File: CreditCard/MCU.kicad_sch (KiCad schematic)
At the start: 21 parts, among them J2 MEM2052-00-195-00-A_REVA, U3 PTS645SK43SMTR92LFS, U4 PTS645SK43SMTR92LFS, U8 ESP32-C6-WROOM-1U-N4, X1 MS1V-T1K-32.768KHZ-12.5PF-20P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

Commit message: manque écran
manque seulement l'écran le reste est ajouter
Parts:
- removed J2: MEM2052-00-195-00-A_REVA, LIB:GCT_MEM2052-00-195-00-A_REVA, symbol MEM2052-00-195-00-A_REVA:MEM2052-00-195-00-A_REVA
- removed U8: ESP32-C6-WROOM-1U-N4, LIB:XCVR_ESP32-C6-WROOM-1U-N4, symbol ESP32-C6-WROOM-1U-N4:ESP32-C6-WROOM-1U-N4
- removed X1: MS1V-T1K-32.768KHZ-12.5PF-20PPM-TA-QC, LIB:XTAL_MS1V-T1K-32.768KHZ-12.5PF-20PPM-TA-QC, symbol LIB:MS1V-T1K-32.768KHZ-12.5PF-20PPM-TA-QC
- added J2: MEM2052-00-195-00-A_REVA, Library:GCT_MEM2052-00-195-00-A_REVA, symbol Library:MEM2052-00-195-00-A_REVA
- added U8: ESP32-C6-WROOM-1U-N4, Library:XCVR_ESP32-C6-WROOM-1U-N4, symbol Library:ESP32-C6-WROOM-1U-N4
- added Y1: MS1V-T1K-32.768KHZ-12.5PF-20PPM-TA-QC, Library:XTAL_MS1V-T1K-32.768KHZ-12.5PF-20PPM-TA-QC, symbol Library:MS1V-T1K-32.768KHZ-12.5PF-20PPM-TA-QC
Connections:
- net 3V3: now also J2.P4 (VDD), U8.2 (3V3)
- net CS_SD: now also J2.P2 (CD/DAT3), U8.20 (IO22)
- net CardDetect_SD: now also J2.P9 (CD_PIN), U8.19 (IO21)
- net D_N: now also U8.13 (IO12)
- net D_P: now also U8.14 (IO13)
- net GND: now also J2.G1 (SHIELD_GND), J2.G2 (SHIELD_GND), J2.G3 (SHIELD_GND), J2.G4 (SHIELD_GND), J2.P6 (VSS), U8.1 (GND), U8.28 (GND__1), U8.29_1 (GND__2), U8.29_2 (GND__3), U8.29_3 (GND__4), U8.29_4 (GND__5), U8.29_5 (GND__6), U8.29_6 (GND__7), U8.29_7 (GND__8), U8.29_8 (GND__9), U8.29_9 (GND__10)
- net GPIO2: now also U8.27 (IO2)
- net GPIO3: now also U8.26 (IO3)
- net GPIO4: now also U8.4 (IO4)
- net GPIO5: now also U8.5 (IO5)
- net GPIO6: now also U8.6 (IO6)
- net GPIO7: now also U8.7 (IO7)
- net IO9: now also U8.15 (IO9)
- net IO_CHG: now also U8.21 (IO23)
- net MCU_EN: now also U8.3 (EN)
- net MISO: now also J2.P7 (DAT0), U8.16 (IO18)
- net MOSI: now also J2.P3 (CMD), U8.17 (IO19)
- net SCK: now also J2.P5 (CLK), U8.11 (IO10)
- net SCL: now also U8.25 (TXD0/GPIO16)
- net SDA: now also U8.24 (RXD0/GPIO17)
- net XTAL_N: now also U8.8 (IO0)
- net XTAL_P: now also U8.9 (IO1)
- net at C12.1, R14.2, R17.2: now also Y1.1
- net at C17.1, R17.1, R20.2: now also Y1.2
- net at R2.1: now also U8.10 (IO8)

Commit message: ajout des gold fingers
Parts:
- removed F1, F2, F4, F5, F6: ~, CommonLib_HORUS:GOLD_FINGERS, symbol LIB:GoldFingers
- added F1, F2, F3, F4: ~, Library:GOLD_FINGERS, symbol Library:GoldFingers
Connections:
- net 3V3: now also F4.1 (GOLDFINGER)
- net IO_CHG: now also F3.1 (GOLDFINGER)
- net SCL: now also F2.1 (GOLDFINGER)
- net SDA: now also F1.1 (GOLDFINGER)

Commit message: connection du audio amp
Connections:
- net SCK: now also U8.23 (IO15); no longer U8.11 (IO10)
- net AudioR: now reaches U8.12 (IO11)
- net AudioCS: now reaches U8.18 (IO20)
- new net AudioL: U8.11 (IO10)
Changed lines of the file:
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@@
+		)
+	)
+	(global_label "AudioL"
+		(shape output)
+		(at 185.42 48.26 0)
+		(fields_autoplaced yes)
+		(effects
+			(font
+				(size 1.27 1.27)
+			)
+			(justify left)
+		)
+		(property "Intersheetrefs" "${INTERSHEET_REFS}"
+			(at 194.5737 48.26 0)
+			(effects
+				(font
+					(size 1.27 1.27)
+				)
+				(justify left)
+				(hide yes)
+			)
 		)
 	)
@@
 		)
 	)
+	(global_label "SCK"
+		(shape output)
+		(at 185.42 58.42 0)
+		(fields_autoplaced yes)
+		(effects
+			(font
+				(size 1.27 1.27)
+			)
+			(justify left)
+		)
+		(property "Intersheetrefs" "${INTERSHEET_REFS}"
+			(at 192.1547 58.42 0)
+			(effects
+				(font
+					(size 1.27 1.27)
+				)
+				(justify left)
+				(hide yes)
+			)
+		)
+	)
 	(global_label "CardDetect_SD"
 		(shape output)
@@
 		)
 	)
+	(global_label "AudioR"
+		(shape output)
+		(at 185.42 50.8 0)
+		(fields_autoplaced yes)
+		(effects
+			(font
+				(size 1.27 1.27)
+			)
+			(justify left)
+		)
+		(property "Intersheetrefs" "${INTERSHEET_REFS}"
+			(at 194.8156 50.8 0)
+			(effects
+				(font
+					(size 1.27 1.27)
+				)
+				(justify left)
+				(hide yes)
+			)
+		)
+	)
 	(global_label "IO_CHG"
 		(shape input)
@@
 		)
 	)
-	(global_label "SCK"
-		(shape output)
-		(at 185.42 48.26 0)
-		(fields_autoplaced yes)
-		(effects
-			(font
-				(size 1.27 1.27)
-			)
-			(justify left)
-		)
-		(property "Intersheetrefs" "${INTERSHEET_REFS}"
-			(at 192.1547 48.26 0)
-			(effects
-				(font
-					(size 1.27 1.27)
-				)
-				(justify left)
-				(hide yes)
-			)
-		)
-	)
 	(global_label "MCU_EN"
 		(shape output)
@@
 				(hide yes)
 			)
+		)
+	)
+	(global_label "AudioCS"
+		(shape output)
+		(at 185.42 71.12 0)
+		(fields_autoplaced yes)
+		(effects
+			(font
+				(size 1.27 1.27)
+			)
+			(justify left)
+		)
+		(property "Intersheetrefs" "${INTERSHEET_REFS}"
+			(at 196.0251 71.12 0)
+			(effects
+				(font
+					(size 1.27 1.27)
+				)
+				(justify left)
+				(hide yes)
+			)

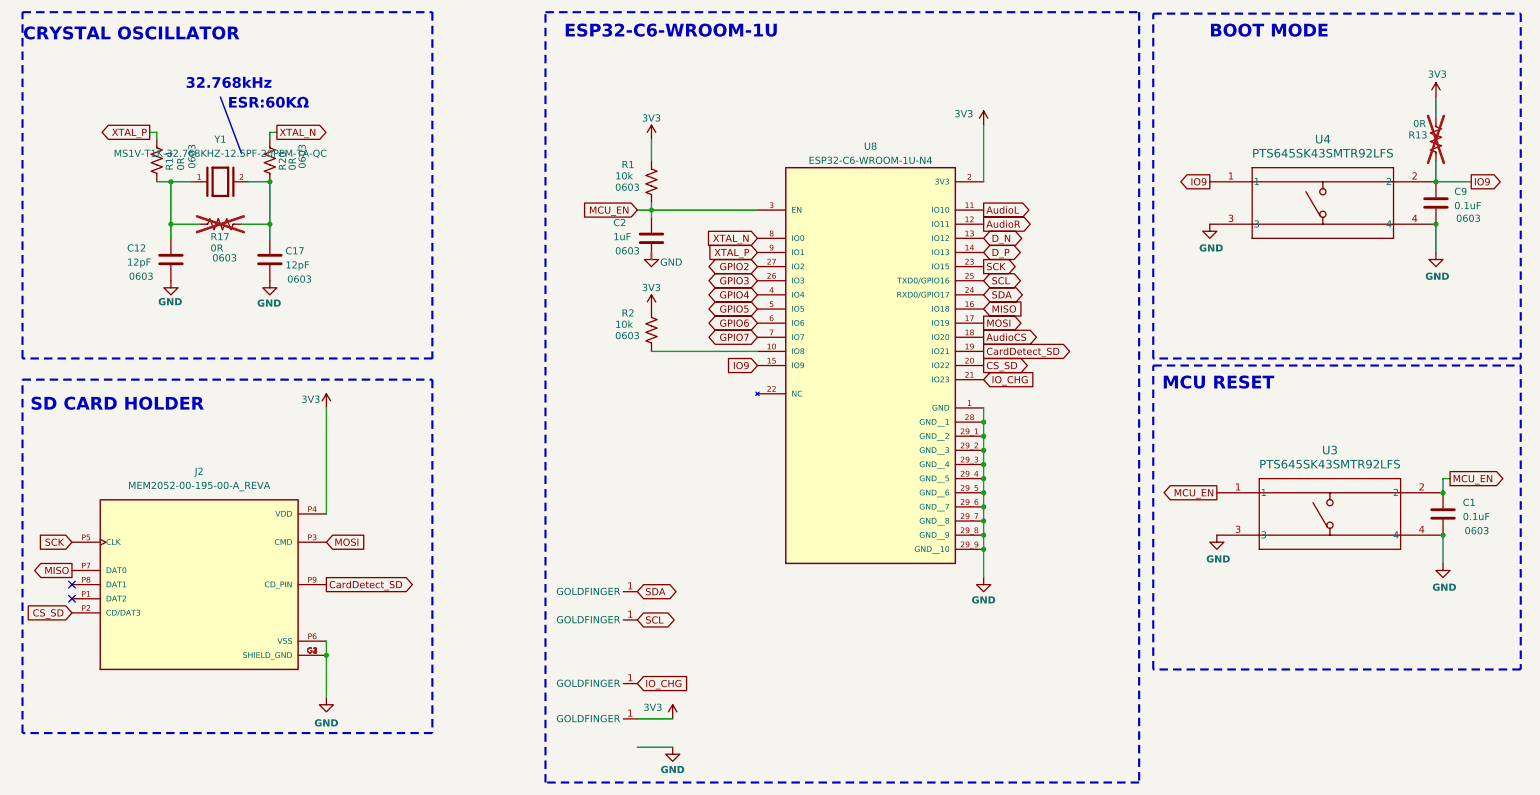
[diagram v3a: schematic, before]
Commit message: ajout du LCD
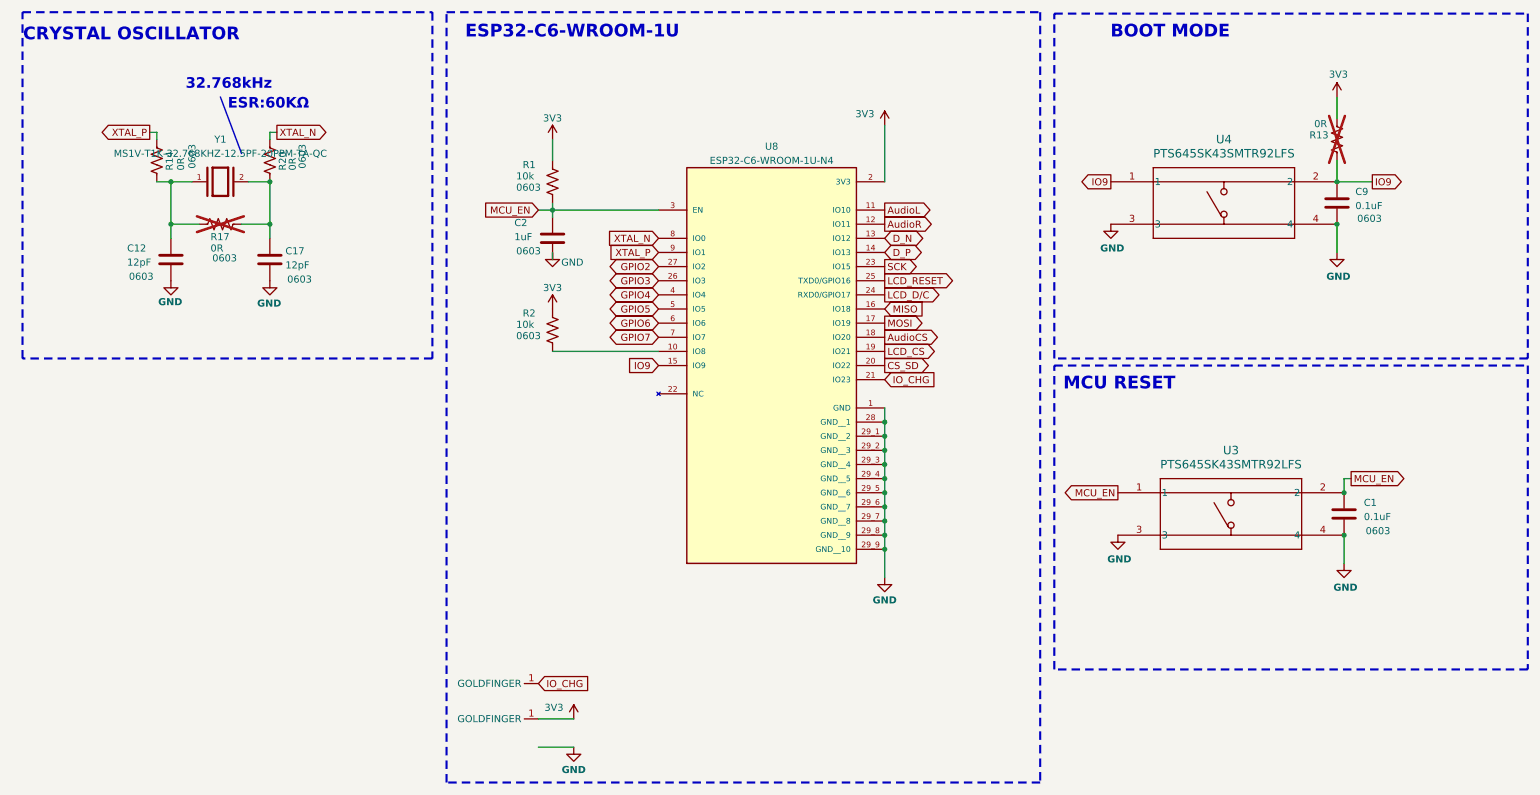
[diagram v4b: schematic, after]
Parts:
- removed F1, F2: ~, Library:GOLD_FINGERS, symbol Library:GoldFingers
- removed J2: MEM2052-00-195-00-A_REVA, Library:GCT_MEM2052-00-195-00-A_REVA, symbol Library:MEM2052-00-195-00-A_REVA
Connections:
- net CardDetect_SD renamed LCD_CS
- net SCL renamed LCD_RESET
- net SDA renamed LCD_D/C
- no-connect marks 2 -> 0
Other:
- note removed: "SD CARD HOLDER"
- moved on the sheet: C1, C2, C9, R1, R13, R2, U3, U4, U8

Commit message: rooting presque fini
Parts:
- removed R14, R20: 0R, Resistor_SMD:R_0603_1608Metric, symbol Device:R_US
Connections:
- net XTAL_N: now also C17.1, R17.1, Y1.2
- net XTAL_P: now also C12.1, R17.2, Y1.1

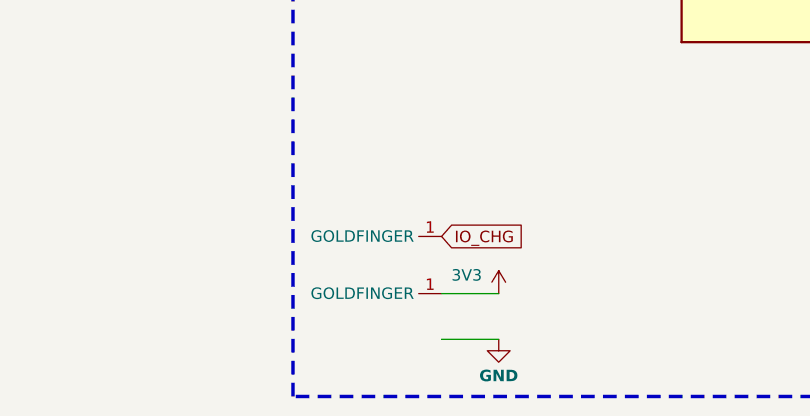
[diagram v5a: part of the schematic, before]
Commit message: gerber crée
pcb terminer
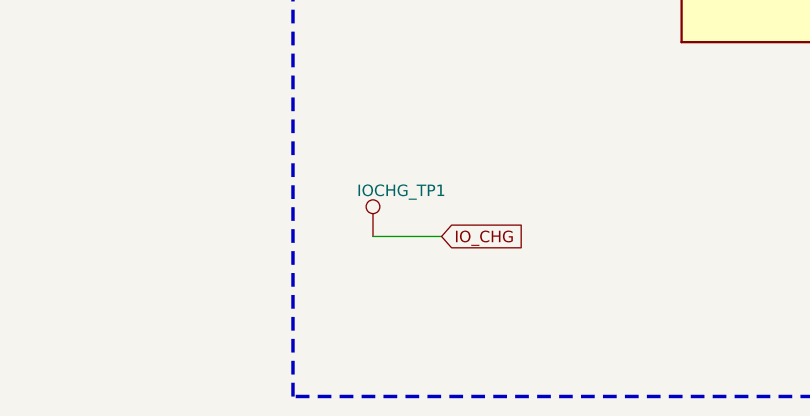
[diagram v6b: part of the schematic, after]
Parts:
- removed F3, F4: ~, Library:GOLD_FINGERS, symbol Library:GoldFingers
- added IOCHG_TP1: TP, TestPoint:TestPoint_Pad_D1.5mm, symbol Connector:TestPoint
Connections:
- net IO_CHG: now also IOCHG_TP1.1
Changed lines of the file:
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@@
 	(wire
 		(pts
-			(xy 107.95 73.66) (xy 127 73.66)
+			(xy 97.79 133.35) (xy 105.41 133.35)
 		)
 		(stroke
@@
 	(wire
 		(pts
-			(xy 248.92 27.94) (xy 248.92 31.75)
+			(xy 107.95 73.66) (xy 127 73.66)
 		)
 		(stroke
@@
 	(wire
 		(pts
-			(xy 248.92 43.18) (xy 255.27 43.18)
+			(xy 248.92 27.94) (xy 248.92 31.75)
 		)
 		(stroke
@@
 	(wire
 		(pts
-			(xy 39.37 43.18) (xy 43.18 43.18)
+			(xy 248.92 43.18) (xy 255.27 43.18)
 		)
 		(stroke
@@
 	(wire
 		(pts
-			(xy 167.64 101.6) (xy 167.64 104.14)
+			(xy 39.37 43.18) (xy 43.18 43.18)
 		)
 		(stroke
@@
 	(wire
 		(pts
-			(xy 251.46 96.52) (xy 250.19 96.52)
+			(xy 167.64 101.6) (xy 167.64 104.14)
 		)
 		(stroke
@@
 	(wire
 		(pts
-			(xy 167.64 106.68) (xy 167.64 109.22)
+			(xy 251.46 96.52) (xy 250.19 96.52)
 		)
 		(stroke
@@
 	(wire
 		(pts
-			(xy 111.76 139.7) (xy 105.41 139.7)
+			(xy 167.64 106.68) (xy 167.64 109.22)
 		)
 		(stroke
@@
 	(wire
 		(pts
-			(xy 105.41 144.78) (xy 111.76 144.78)
-		)
-		(stroke
-			(width 0)
-			(type default)
-		)
-	)
-	(wire
-		(pts
 			(xy 107.95 57.15) (xy 107.95 55.88)
 		)
@@
 	)
 	(symbol
-		(lib_id "power:+3.3V")
-		(at 111.76 139.7 0)
-		(unit 1)
-		(exclude_from_sim no)
-		(in_bom yes)
-		(on_board yes)
-		(dnp no)
-		(property "Reference" "#PWR032"
-			(at 111.76 143.51 0)
-			(effects
-				(font
-					(size 1.27 1.27)
-				)
-				(hide yes)
-			)
-		)
-		(property "Value" "3V3"
-			(at 108.204 137.668 0)
-			(effects
-				(font
-					(size 1.27 1.27)
-				)
-			)
-		)
-		(property "Footprint" ""
-			(at 111.76 139.7 0)
-			(effects
-				(font
-					(size 1.27 1.27)
-				)
-				(hide yes)
-			)
-		)
-		(property "Datasheet" ""
-			(at 111.76 139.7 0)
-			(effects
-				(font
-					(size 1.27 1.27)
-				)
-				(hide yes)
-			)
-		)
-		(property "Description" "Power symbol creates a global label with name \"+3.3V\""
-			(at 111.76 139.7 0)
-			(effects
-				(font
-					(size 1.27 1.27)
-				)
-				(hide yes)
-			)
-		)
-		(pin "1"
-		)
-		(instances
-			(project "CreditCard"
-				(path "/374dba13-75d6-44a0-b8b2-0ca0aa70330e/e30e25a5-3034-4dd4-af11-e901f7261987"
-					(reference "#PWR032")
-					(unit 1)
-				)
-			)
-		)
-	)
-	(symbol
 		(lib_id "Device:C")
 		(at 107.95 53.34 0)
@@
 	)
 	(symbol
-		(lib_id "Library:GoldFingers")
-		(at 105.41 139.7 180)
-		(unit 1)
-		(exclude_from_sim no)
-		(in_bom yes)
-		(on_board yes)
-		(dnp no)
-		(fields_autoplaced yes)
-		(property "Reference" "F4"
-			(at 105.41 141.732 0)
-			(effects
-				(font
-					(size 1.27 1.27)
-				)
-				(hide yes)
-			)
-		)
-		(property "Value" "~"
-			(at 102.87 137.16 0)
-			(effects
-				(font
-					(size 1.27 1.27)
-				)
-			)
-		)
-		(property "Footprint" "Library:GOLD_FINGERS"
-			(at 104.648 135.89 0)
-			(effects
-				(font
-					(size 1.27 1.27)
-				)
-				(hide yes)
-			)
-		)
-		(property "Datasheet" ""
-			(at 105.41 139.7 0)
-			(effects
-				(font
-					(size 1.27 1.27)
-				)
-				(hide yes)
-			)
-		)
-		(property "Description" ""
-			(at 105.41 139.7 0)
-			(effects
-				(font
-					(size 1.27 1.27)
-				)
-				(hide yes)
-			)
-		)
-		(pin "1"
-		)
-		(instances
-			(project ""
-				(path "/374dba13-75d6-44a0-b8b2-0ca0aa70330e/e30e25a5-3034-4dd4-af11-e901f7261987"
-					(reference "F4")
-					(unit 1)
-				)
-			)
-		)
-	)
-	(symbol
 		(lib_id "Device:R_US")
 		(at 248.92 35.56 180)
@@
 	(symbol
 		(lib_id "power:GND")
-		(at 111.76 144.78 0)
-		(unit 1)
-		(exclude_from_sim no)
-		(in_bom yes)
-		(on_board yes)
-		(dnp no)
-		(property "Reference" "#PWR041"
-			(at 111.76 151.13 0)
-			(effects
-				(font
-					(size 1.27 1.27)
-				)
-				(hide yes)
-			)
-		)
-		(property "Value" "GND"
-			(at 111.76 148.844 0)
-			(effects
-				(font
-					(size 1.27 1.27)
-					(bold yes)
-				)
-			)
-		)
-		(property "Footprint" ""
-			(at 111.76 144.78 0)
-			(effects
-				(font
-					(size 1.27 1.27)
-				)
-				(hide yes)
-			)
-		)
-		(property "Datasheet" ""
-			(at 111.76 144.78 0)
-			(effects
-				(font
-					(size 1.27 1.27)
-				)
-				(hide yes)
-			)
-		)
-		(property "Description" "Power symbol creates a global label with name \"GND\" , ground"
-			(at 111.76 144.78 0)
-			(effects
-				(font
-					(size 1.27 1.27)
-				)
-				(hide yes)
-			)
-		)
-		(pin "1"
-		)
-		(instances
-			(project "CreditCard"
-				(path "/374dba13-75d6-44a0-b8b2-0ca0aa70330e/e30e25a5-3034-4dd4-af11-e901f7261987"
-					(reference "#PWR041")
-					(unit 1)
-				)
-			)
-		)
-	)
-	(symbol
-		(lib_id "power:GND")
 		(at 39.37 60.96 0)
 		(unit 1)
@@
 	)
 	(symbol
-		(lib_id "Library:GoldFingers")
-		(at 105.41 133.35 180)
-		(unit 1)
-		(exclude_from_sim no)
-		(in_bom yes)
-		(on_board yes)
-		(dnp no)
-		(fields_autoplaced yes)
-		(property "Reference" "F3"
-			(at 105.41 135.382 0)
-			(effects
-				(font
-					(size 1.27 1.27)
-				)
-				(hide yes)
-			)
-		)
-		(property "Value" "~"
-			(at 102.87 130.81 0)
-			(effects
-				(font
-					(size 1.27 1.27)
-				)
-			)
-		)
-		(property "Footprint" "Library:GOLD_FINGERS"
-			(at 104.648 129.54 0)
-			(effects
-				(font
-					(size 1.27 1.27)
-				)
-				(hide yes)
-			)
-		)
-		(property "Datasheet" ""
-			(at 105.41 133.35 0)
-			(effects
-				(font
-					(size 1.27 1.27)
-				)
-				(hide yes)
-			)
-		)
-		(property "Description" ""
-			(at 105.41 133.35 0)
-			(effects
-				(font
-					(size 1.27 1.27)
-				)
-				(hide yes)
-			)
-		)
-		(pin "1"
-		)
-		(instances
-			(project ""
-				(path "/374dba13-75d6-44a0-b8b2-0ca0aa70330e/e30e25a5-3034-4dd4-af11-e901f7261987"
-					(reference "F3")
-					(unit 1)
-				)
-			)
-		)
-	)
-	(symbol
 		(lib_id "power:GND")
 		(at 107.95 55.88 0)
@@
 					(unit 1)
 				)
+			)
+		)
+	)
+	(symbol
+		(lib_id "Connector:TestPoint")
+		(at 97.79 133.35 0)
+		(unit 1)
+		(exclude_from_sim no)
+		(in_bom yes)
+		(on_board yes)
+		(dnp no)
+		(property "Reference" "IOCHG_TP1"
+			(at 96.012 128.27 0)
+			(effects
+				(font
+					(size 1.27 1.27)
+				)
+				(justify left)
+			)
+		)
+		(property "Value" "TP"
+			(at 99.314 131.318 0)
+			(effects
+				(font
+					(size 1.27 1.27)
+				)
+				(justify left)
+				(hide yes)
+			)
+		)
+		(property "Footprint" "TestPoint:TestPoint_Pad_D1.5mm"
+			(at 102.87 133.35 0)
+			(effects
+				(font
+					(size 1.27 1.27)
+				)
+				(hide yes)
+			)
+		)
+		(property "Datasheet" "~"
+			(at 102.87 133.35 0)
+			(effects
+				(font
+					(size 1.27 1.27)
+				)
+				(hide yes)
+			)
+		)
+		(property "Description" "test point"
+			(at 97.79 133.35 0)
+			(effects
+				(font
+					(size 1.27 1.27)
+				)
+				(hide yes)
+			)
+		)
+		(pin "1"
+		)
+		(instances
+			(project "CreditCard"
+				(path "/374dba13-75d6-44a0-b8b2-0ca0aa70330e/e30e25a5-3034-4dd4-af11-e901f7261987"
+					(reference "IOCHG_TP1")
+					(unit 1)
+				)
